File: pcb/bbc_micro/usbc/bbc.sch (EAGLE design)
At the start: 29 parts, among them U2 LM2776

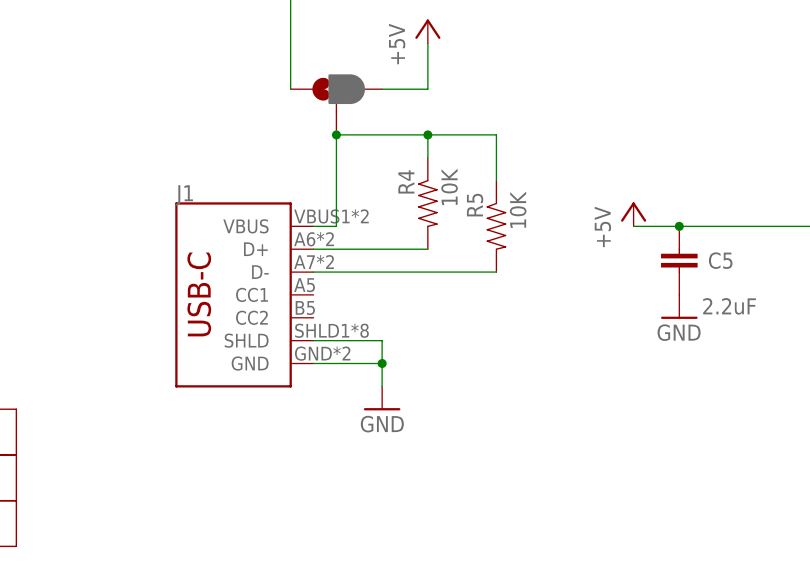
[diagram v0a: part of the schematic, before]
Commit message: adjusted jumper angle, fixed pin bug
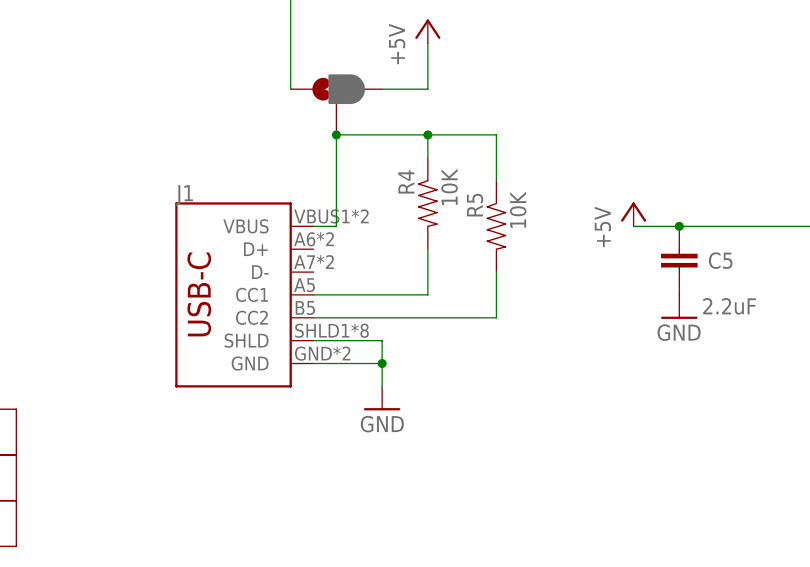
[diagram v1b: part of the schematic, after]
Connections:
- net N$8: now also J1.CC2, R5.2; no longer J1.D+, R4.2
- net N$9: now also J1.CC1, R4.2; no longer J1.D-, R5.2
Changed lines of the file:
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@@
 <net name="N$8" class="0">
 <segment>
-<pinref part="J1" gate="J1" pin="D+"/>
-<pinref part="R4" gate="G$1" pin="2"/>
-<wire x1="218.44" y1="160.02" x2="231.14" y2="160.02" width="0.1524" layer="91"/>
+<pinref part="R5" gate="G$1" pin="2"/>
+<pinref part="J1" gate="J1" pin="CC2"/>
+<wire x1="238.76" y1="157.48" x2="238.76" y2="152.4" width="0.1524" layer="91"/>
+<wire x1="238.76" y1="152.4" x2="218.44" y2="152.4" width="0.1524" layer="91"/>
 </segment>
 </net>
 <net name="N$9" class="0">
 <segment>
-<pinref part="J1" gate="J1" pin="D-"/>
-<pinref part="R5" gate="G$1" pin="2"/>
-<wire x1="218.44" y1="157.48" x2="238.76" y2="157.48" width="0.1524" layer="91"/>
+<pinref part="R4" gate="G$1" pin="2"/>
+<pinref part="J1" gate="J1" pin="CC1"/>
+<wire x1="231.14" y1="160.02" x2="231.14" y2="154.94" width="0.1524" layer="91"/>
+<wire x1="231.14" y1="154.94" x2="218.44" y2="154.94" width="0.1524" layer="91"/>
 </segment>
 </net>
